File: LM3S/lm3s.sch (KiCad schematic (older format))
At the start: 49 parts, among them J1 DC_POWER_JACK, P1 CONN_4X2, U1 LM3S6965, U2 J00-0062NL, U3 1117, X1 32.768Khz, X2 25Mhz, X3 8Mhz

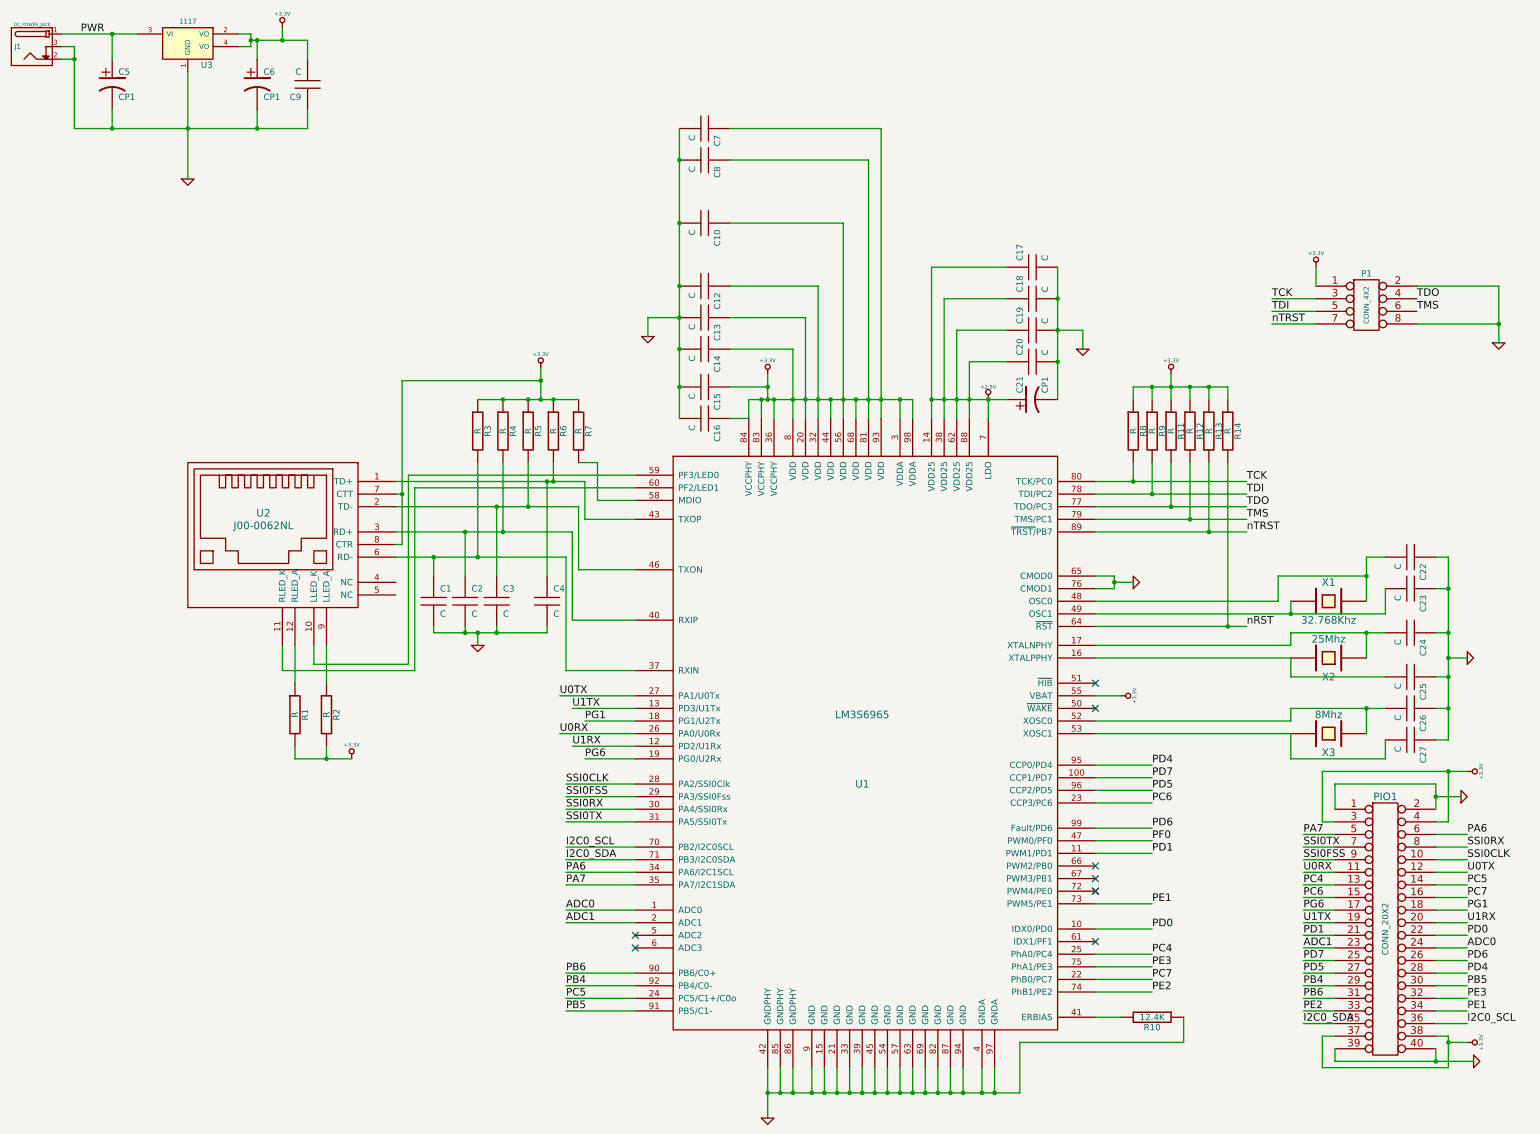
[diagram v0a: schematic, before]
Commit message: Terminado LM3S board. Modificadas las placas para fabricación con ourpcb. GERBERS para our PCB en una sola placa
Signed-off-by: Martin Ribelotta <martinribelotta@gmail.com>
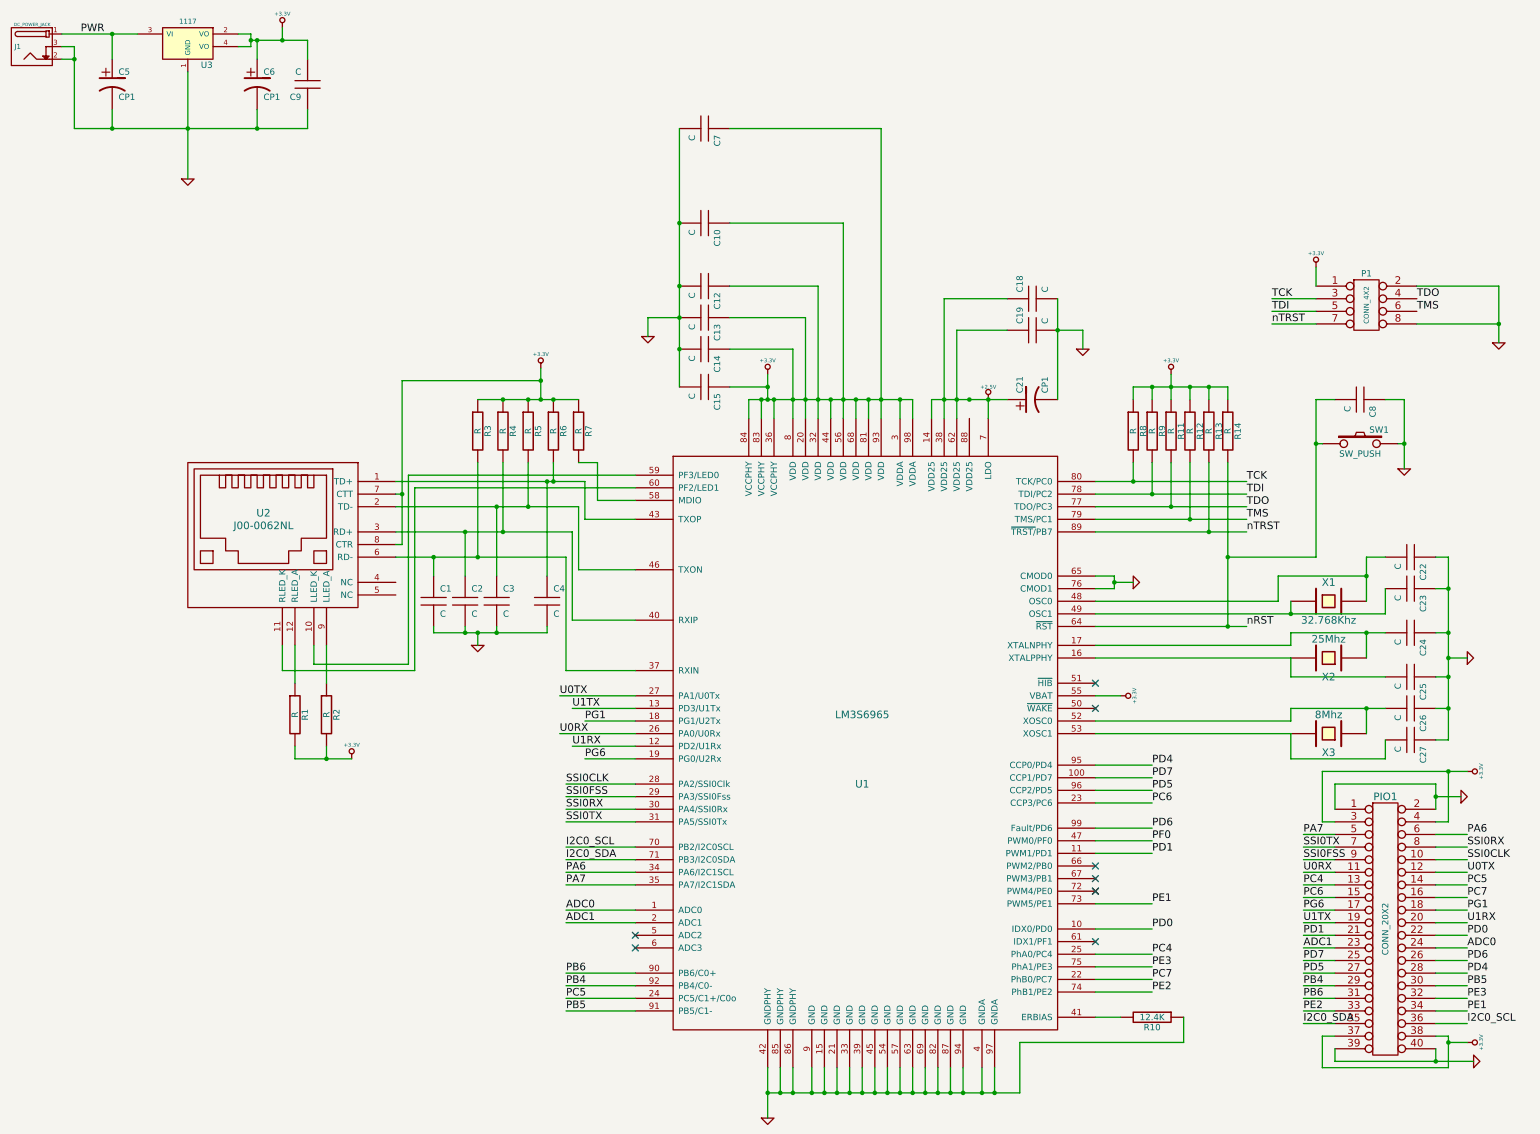
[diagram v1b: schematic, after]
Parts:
- removed C16, C17, C20: C, symbol C
- added SW1: SW_PUSH, symbol SW_PUSH
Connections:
- net +2.5V: no longer U1.88 (VDD25)
- net +3.3V: no longer C8.1
- net GND: now also C8.1, SW1.2; no longer C8.2
- net nRST: now also C8.2, SW1.1
